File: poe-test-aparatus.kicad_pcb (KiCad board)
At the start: 2 copper layers, 65.1 x 56 mm, 32 parts, among them J1 Power Injector, J2 PoE Header, U1 MP8007, U2 POE70P-12L

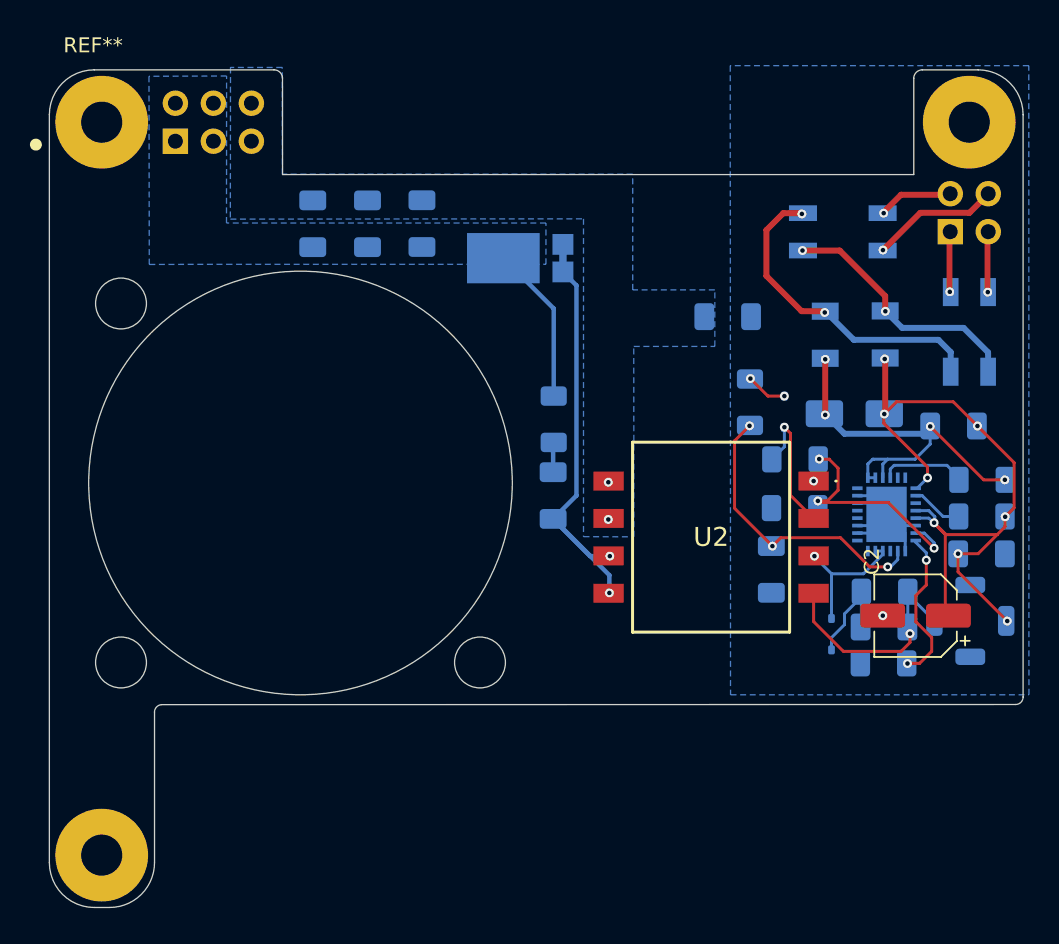
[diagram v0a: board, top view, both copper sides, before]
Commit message: Rework with better layout and resistors fix tests
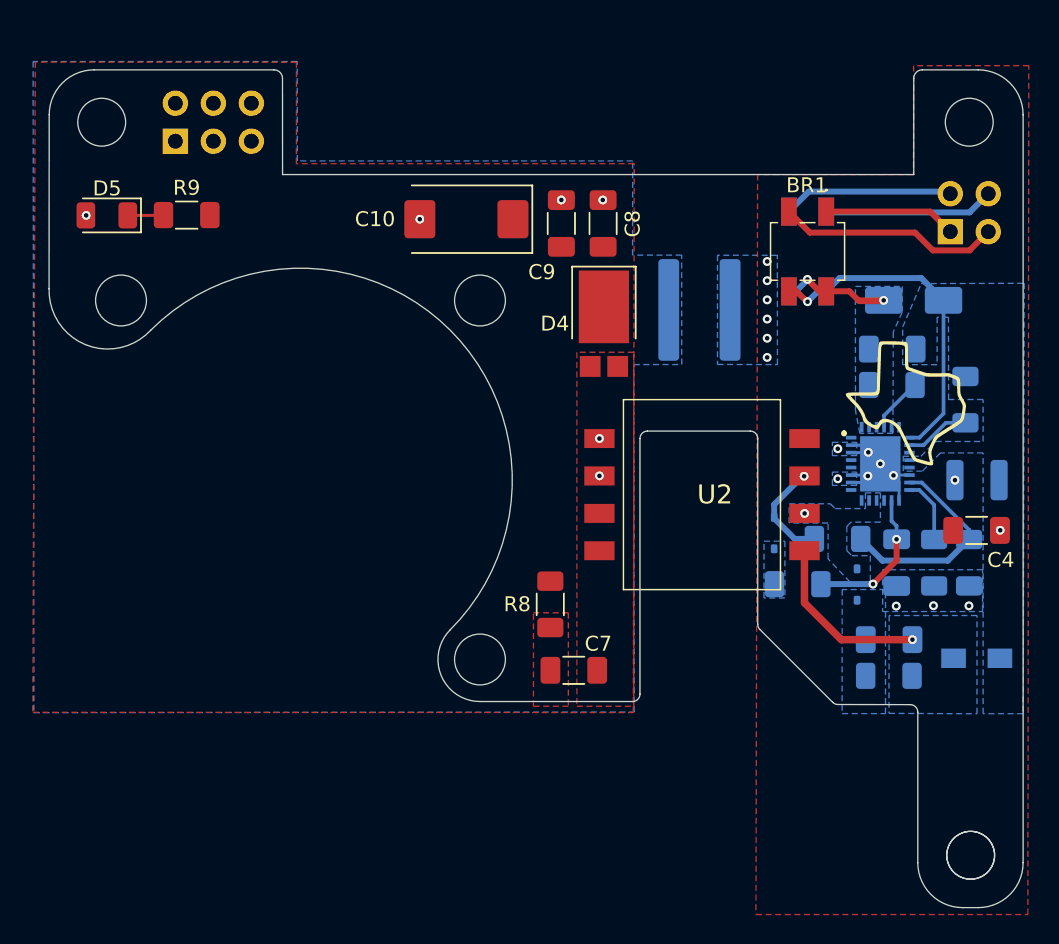
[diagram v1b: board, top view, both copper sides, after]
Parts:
- removed FB1, FB2: 240R, PowerManagement:BLM31KN102BH1L
- removed REF**: PoE_Hat, RpiHats:MODULE_RASPBERRY_PI_4B_4GB
- added ?: , , F.Cu at (162.2, 127.9)
- added D5: PWR, LED_SMD:LED_1206_3216Metric, F.Cu at (104.4, 85.2)
- added H1: MountingHole, MountingHole:MountingHole_3.2mm_M3_ISO14580, F.Cu at (104.1, 78.9)
- added H2: MountingHole, MountingHole:MountingHole_3.2mm_M3_ISO14580, F.Cu at (162.1, 78.9)
- added H3: MountingHole, MountingHole:MountingHole_3.2mm_M3_ISO14580, F.Cu at (162.2, 127.9)
- added R9: 1k, Resistor_SMD:R_1206_3216Metric_Pad1.30x1.75mm_HandSolder, F.Cu at (109.8, 85.1)
- BR1, C4, C7: moved to F.Cu
- C10: value 220uF -> 470uF; footprint Capacitor_SMD:C_1206_3216Metric_Pad1.33x1.80mm_HandSolder -> Capacitor_Tantalum_SMD:CP_EIA-7343-43_Kemet-X; moved to F.Cu
- C2: footprint Capacitor_SMD:CP_Elec_5x5.4 -> Capacitor_SMD:C_1210_3225Metric; moved to B.Cu
- C6: value 2.2nF/2000V -> 2.2nF; footprint Capacitor_SMD:C_1206_3216Metric_Pad1.33x1.80mm_HandSolder -> Capacitor_SMD:C_1825_4564Metric
- C8, C9: value 22uF -> 47uF; moved to F.Cu
- D4: value SBR8U60P5 -> SBR8U60P5-7; moved to F.Cu
- L1: footprint Inductor_SMD:L_Bourns_SRU5016_5.2x5.2mm -> InductorAlt:INDPM3532X120N
- R2: value 41.2 -> 41.2R
- R3: value 52k -> 64.9k
- R4: value 20k -> 17.8k
- R5: value 49.9k -> 110k
- R7: value 1k -> 5.1k
- R8: value 20k -> 20R; moved to F.Cu
- U2: value POE70P-12L -> POE70P-50L; footprint PoweredDevices:POE70P12LD -> PoweredDevices:POE70P50LD
- moved C9 13.0 mm to (134.8, 85.7)
- moved R7 12.6 mm to (150.6, 109.8), turned to 0 degrees
- moved R8 12.4 mm to (134.1, 111.2)
- moved R4 12.2 mm to (162.1, 108.4), turned to -90 degrees
- moved C8 12.1 mm to (137.6, 85.7)
- moved BR1 12.1 mm to (151.3, 87.6), turned to 0 degrees
- moved C7 11.8 mm to (135.6, 115.6), turned to 0 degrees
- moved C10 10.3 mm to (128.4, 85.4), turned to 180 degrees
- moved C2 9.95 mm to (162.6, 102.9)
- moved R2 8.75 mm to (156.9, 96.5), turned to 0 degrees
- moved D1 8.55 mm to (158.3, 90.8)
- moved C3 8.39 mm to (157.2, 108.4)
- moved D3 8.13 mm to (149.0, 106.4), turned to 90 degrees
- moved R1 7.89 mm to (161.8, 97.5), turned to -90 degrees
- moved R3 7.53 mm to (159.7, 108.4), turned to -90 degrees
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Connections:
- net /+5V@2.5A renamed /+5V@1.4A
- net /TR0_TAP renamed /+
- C1 pad 1: Net-(D1-A1) -> Net-(BR1-~_2)
- C1 pad 2: Net-(D1-A2) -> Net-(BR1-~_1)
- C2 pad 1: Net-(D1-A1) -> Net-(BR1-~_2)
- C4 pad 1: Net-(D1-A1) -> Net-(BR1-~_2)
- D1 pad 1: Net-(D1-A1) -> Net-(BR1-~_2)
- D1 pad 2: Net-(D1-A2) -> Net-(BR1-~_1)
- L1 pad 1: Net-(D1-A1) -> Net-(BR1-~_2)
- R1 pad 1: Net-(D1-A1) -> Net-(BR1-~_2)
- R2 pad 1: Net-(D1-A2) -> Net-(BR1-~_1)
- U1 pad 1: Net-(D1-A1) -> Net-(BR1-~_2)
- U1 pad 23: Net-(D1-A2) -> Net-(BR1-~_1)
- U1 pad 24: Net-(D1-A2) -> Net-(BR1-~_1)
- U1 pad 25: Net-(D1-A2) -> Net-(BR1-~_1)
- U1 pad 4: Net-(D1-A1) -> Net-(BR1-~_2)
- U1 pad 5: Net-(D1-A1) -> Net-(BR1-~_2)
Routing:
- net Net-(D1-A1): track 49.0 -> 0.00 mm, vias 8 -> 0
- net Net-(D4-A): track 30.7 -> 0.00 mm, vias 2 -> 0
- net Net-(D1-A2): track 26.0 -> 0.00 mm, vias 4 -> 0
- net Net-(BR1-~_1): track 21.5 -> 9.04 mm
- net /TR1_TAP: track 3.93 -> 14.9 mm, vias 1 -> 0
- net /+5V@1.4A: track 10.6 -> 0.00 mm
- net Net-(U1-VCC): track 19.7 -> 9.88 mm, vias 3 -> 2
- net Net-(D2-A): track 9.42 -> 0.00 mm
- net GNDPWR: track 6.20 -> 14.7 mm, vias 2 -> 16
- net Net-(D2-K): track 6.68 -> 0.00 mm
- net /TR2_TAP: track 4.88 -> 11.4 mm, vias 1 -> 0
- net Net-(U1-ILIM): track 10.4 -> 4.38 mm, vias 2 -> 0
- net Net-(BR1-~_2): track 17.1 -> 22.5 mm
- net /+: track 3.89 -> 8.85 mm, vias 1 -> 0
- net Net-(U2-P-): track 14.9 -> 11.7 mm
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- added copper zone on F.Cu, net /+5V@1.4A
- added copper zone on F.Cu, net GNDPWR
- added copper zone on B.Cu, net Net-(BR1-~_1)
- added copper zone on B.Cu, net Net-(BR1-~_2)
- added copper zone on F.Cu, net Net-(C7-Pad1)
- added copper zone on B.Cu, net Net-(D2-A)
- added copper zone on B.Cu, net Net-(D2-K)
- added copper zone on B.Cu, net Net-(D3-K)
- added copper zone on F.Cu, net Net-(D4-A)
- added copper zone on B.Cu, net Net-(U2-P-)
- removed copper zone on B.Cu, net /+5V@1.4A
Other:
- outline, holes or cut-outs redrawn

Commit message: moderate updates
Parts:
- removed ?: , 
- removed L1: 10uH 1A, InductorAlt:INDPM3532X120N
- added C11: 10uF, Capacitor_SMD:C_1210_3225Metric, F.Cu at (162.5, 99.6)
- added J3: Conn_01x02_Pin, Connector_JST:JST_SH_SM02B-SRSS-TB_1x02-1MP_P1.00mm_Horizontal, B.Cu at (136.7, 113.7)
- C2: value 47uF -> 10uF; moved to F.Cu
- R3: value 64.9k -> 49.9k
- R7: value 5.1k -> 1k
- moved D5 54.5 mm to (157.4, 97.9), turned to 0 degrees
- moved R9 51.2 mm to (160.2, 93.8), turned to 180 degrees
- moved C7 3.04 mm to (135.3, 112.5)
- moved R6 2.43 mm to (154.6, 114.8), turned to 90 degrees
- moved R8 2.37 mm to (134.0, 108.8)
- moved C5 1.30 mm to (157.0, 114.8), turned to 90 degrees
- moved C2 0.22 mm to (162.5, 103.0)
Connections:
- C5 pad 1: Net-(U2-P-) -> Net-(BR1-~_2)
- D5 pad 2: GND -> Net-(D5-K)
- R6 pad 1: Net-(U2-P-) -> Net-(BR1-~_2)
- R9 pad 1: Net-(D5-A) -> Net-(BR1-~_2)
- R9 pad 2: /+5V@1.4A -> Net-(D5-A)
- U1 pad 14: (no net) -> GNDPWR
- U1 pad 15: (no net) -> GNDPWR
- U1 pad 19: (no net) -> GNDPWR
- U1 pad 22: (no net) -> GNDPWR
- U1 pad 27: unconnected-(U1-T2P-Pad27) -> Net-(D5-K)
- U2 pad 4: Net-(U2-P-) -> Net-(BR1-~_2)
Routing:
- net GNDPWR: track 14.7 -> 1.35 mm, vias 16 -> 44
- net Net-(U2-P-): track 11.7 -> 0.00 mm, vias 1 -> 0
- net Net-(D3-A): track 7.17 -> 0.00 mm, vias 1 -> 3
- net Net-(BR1-~_2): track 22.5 -> 26.2 mm, vias 2 -> 12
- net Net-(D5-K): track 0.00 -> 2.89 mm, vias 0 -> 1
- net Net-(D5-A): track 2.40 -> 5.26 mm
- net Net-(D2-A): vias 1 -> 3
- net GND: vias 6 -> 9
- net /+5V@1.4A: vias 0 -> 1
- net (no net): vias 0 -> 6
- added copper zone on B.Cu, net Net-(D3-A)
- removed copper zone on B.Cu, net Net-(U2-P-)
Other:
- board text added: "PWR"
- board text added: "{ "ViaStitching": "0.2", "stitch_zone_0": { "HSpacing": "1", "VSpacing": ".25", "Clearance": "0.1", "Randomize": true } }"
- board text added: "{ "ViaStitching": "0.2", "stitch_zone_0": { "HSpacing": "1", "VSpacing": ".5", "Clearance": "0", "Randomize": true } }"

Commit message: Final clean up for now
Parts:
- moved R4 4.77 mm to (161.8, 103.6)
- moved R3 0.20 mm to (159.5, 108.4)
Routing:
- net Net-(U1-ILIM): track 4.38 -> 0.00 mm
- net Net-(BR1-~_2): track 26.2 -> 22.5 mm, vias 12 -> 26
- net Net-(U1-FB1): track 14.2 -> 17.6 mm
- net /+5V@1.4A: track 0.00 -> 1.27 mm
- net GNDPWR: vias 44 -> 59
- net GND: vias 9 -> 13
- net (no net): vias 6 -> 0
- added copper zone on F.Cu, net Net-(BR1-~_2)
- added copper zone on F.Cu, net Net-(D2-A)
- added copper zone on F.Cu, net Net-(D3-A)
- added copper zone on B.Cu, net Net-(U1-ILIM)

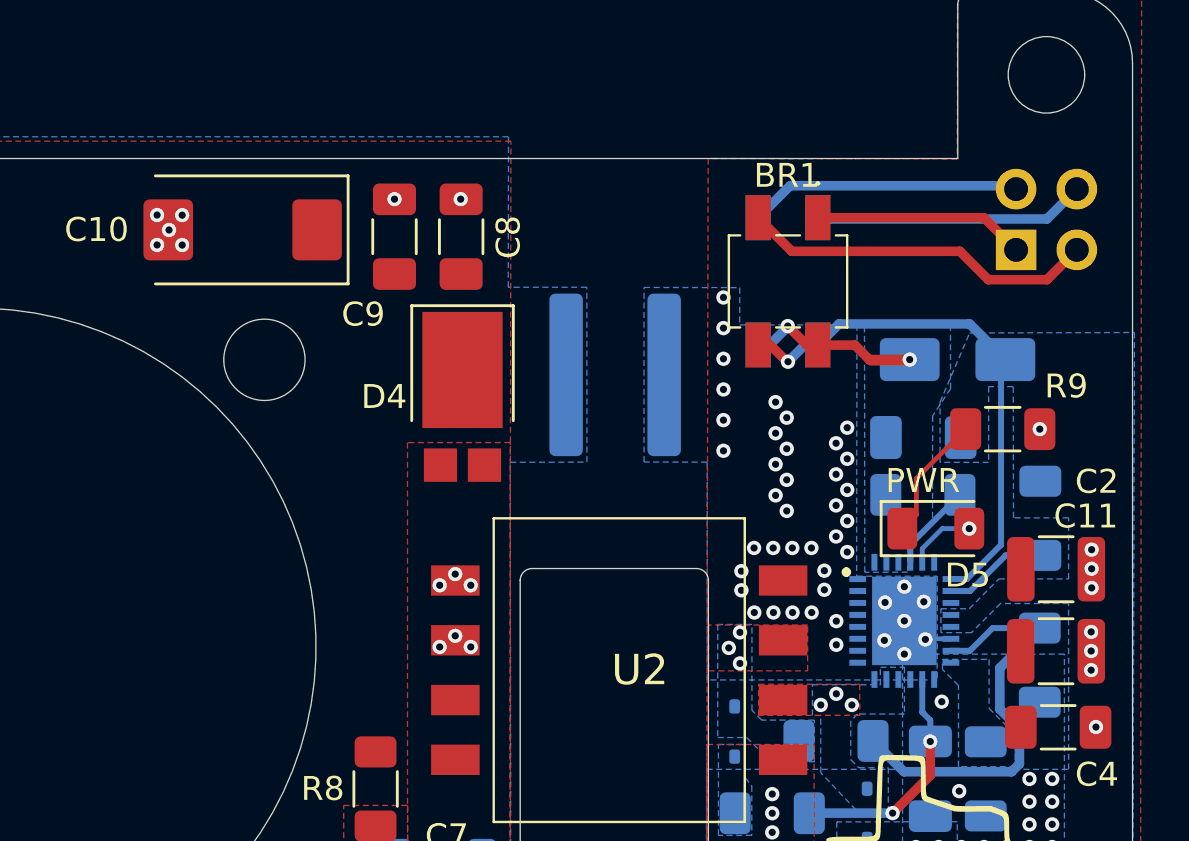
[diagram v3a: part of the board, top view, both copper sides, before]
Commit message: Fixed flipped rectifier diode input
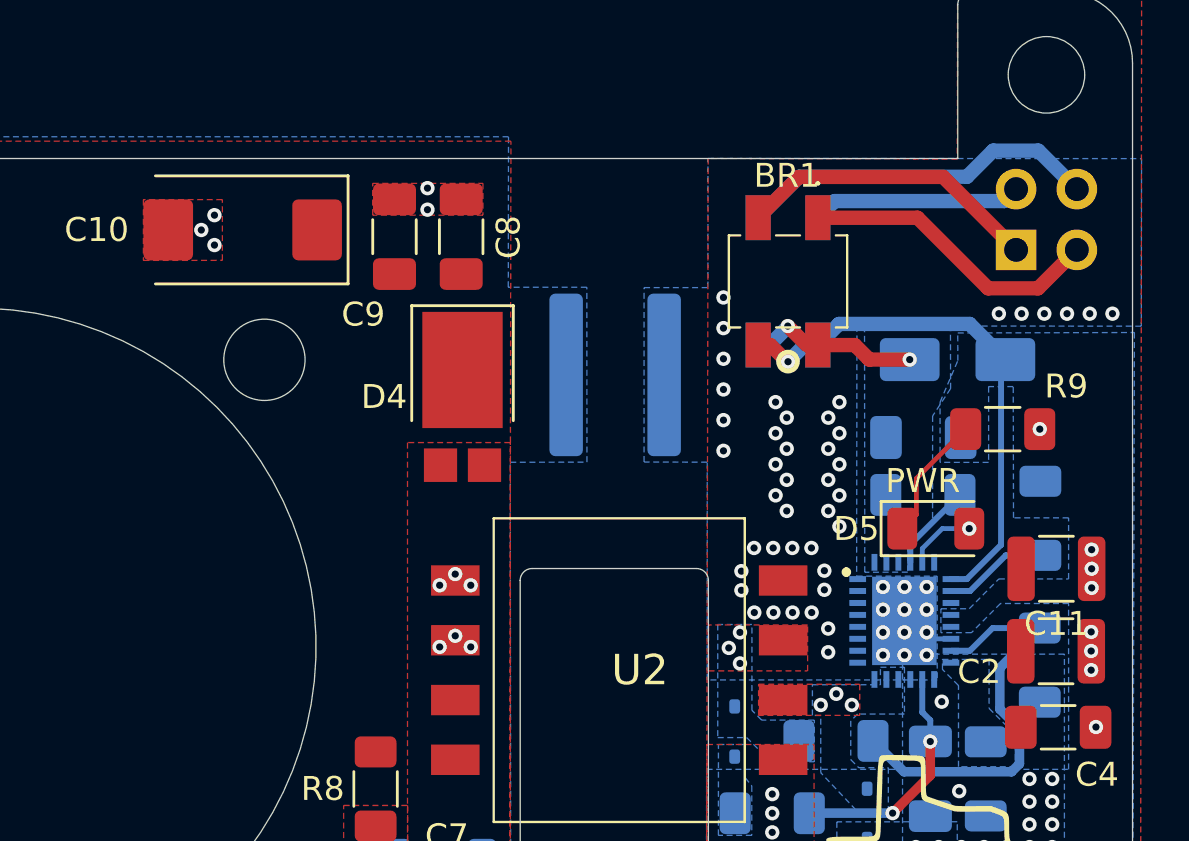
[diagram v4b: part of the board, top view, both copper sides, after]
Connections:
- BR1 pad 3: /TR1_TAP -> /TR0_TAP
- BR2 pad 1: /TR2_TAP -> /TR3_TAP
- BR2 pad 3: /TR3_TAP -> /TR2_TAP
- J2 pad 1: /+ -> /TR0_TAP
- J2 pad 3: /TR1_TAP -> /+
- U1 pad 14: GNDPWR -> (no net)
- U1 pad 15: GNDPWR -> (no net)
- U1 pad 19: GNDPWR -> (no net)
- U1 pad 22: GNDPWR -> (no net)
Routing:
- net /TR1_TAP: track 14.9 -> 0.00 mm
- net /TR0_TAP: track 0.00 -> 12.8 mm
- net /+: track 8.85 -> 12.7 mm
- net /TR3_TAP: track 11.4 -> 15.2 mm
- net /TR2_TAP: track 11.4 -> 8.79 mm
- net Net-(BR1-~_1): track 9.04 -> 7.45 mm
- net GNDPWR: vias 59 -> 70
- net GND: vias 13 -> 11
- added copper zone on F.Cu, net GND
